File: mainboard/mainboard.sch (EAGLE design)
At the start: 12 parts, among them IC1 ATMEGA168-PU

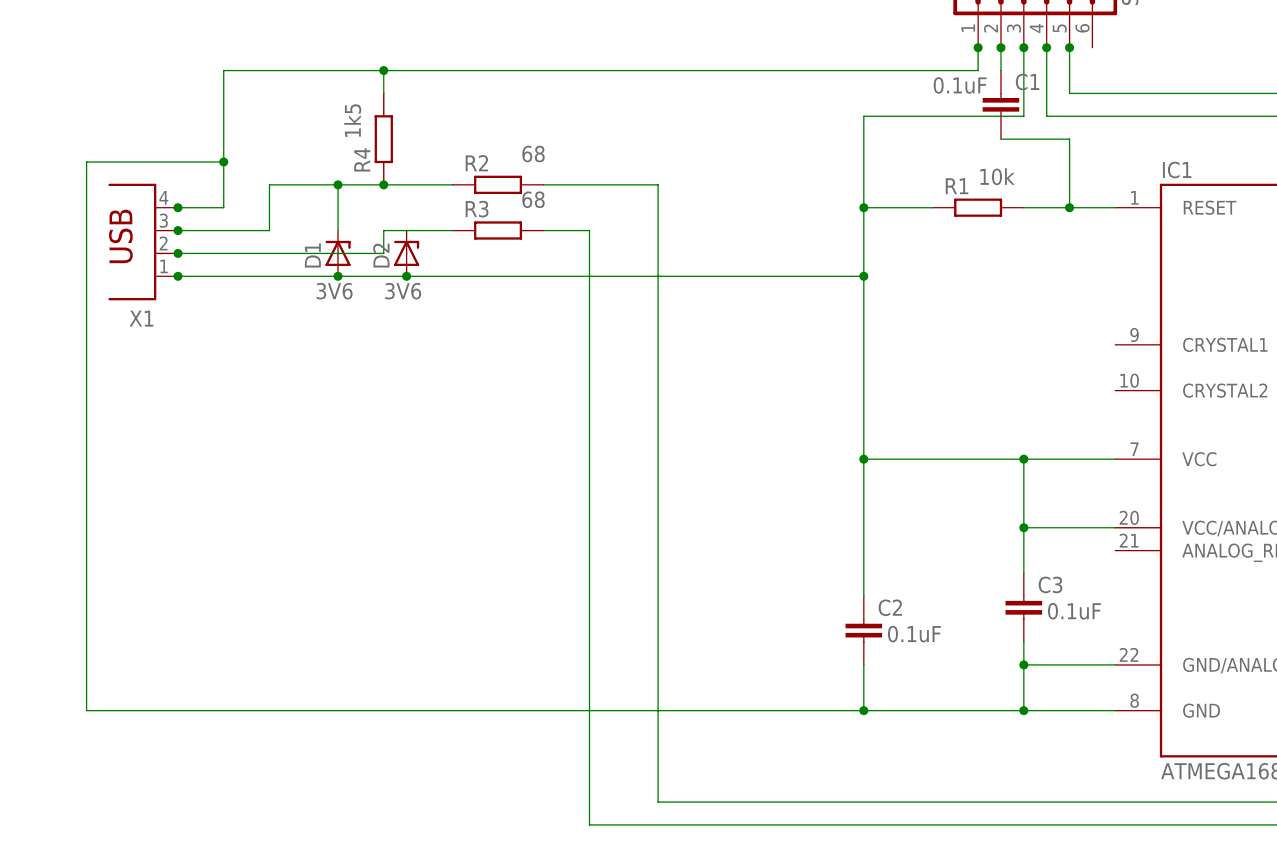
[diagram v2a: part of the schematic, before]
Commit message: added crystal, should run at 12mhz
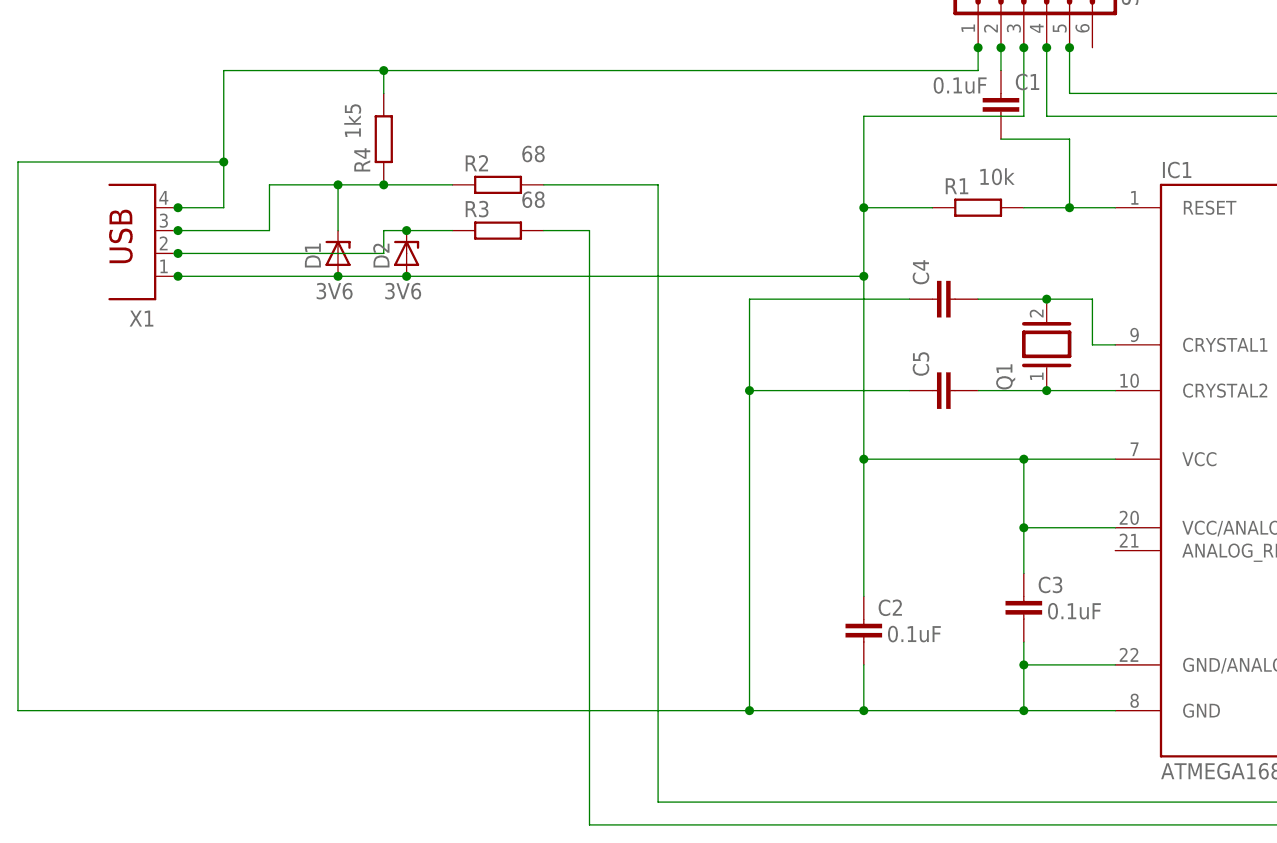
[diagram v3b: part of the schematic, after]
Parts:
- added C4, C5: (no value), capacitor-wima:C2,5-3
- added Q1: (no value), special:XTAL/S
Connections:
- new net N$12: C5.2, IC1.CRYSTAL2, Q1.1
- new net N$9: C2.2, C3.2, C4.1, C5.1, IC1.GND, IC1.GND/ANALOG, R4.2, SV1.1, X1.4
- net N$5: now also D2.C
- net N$8: now also C4.2, IC1.CRYSTAL1, Q1.2; no longer C2.2, C3.2, IC1.GND, IC1.GND/ANALOG, R4.2, SV1.1, X1.4

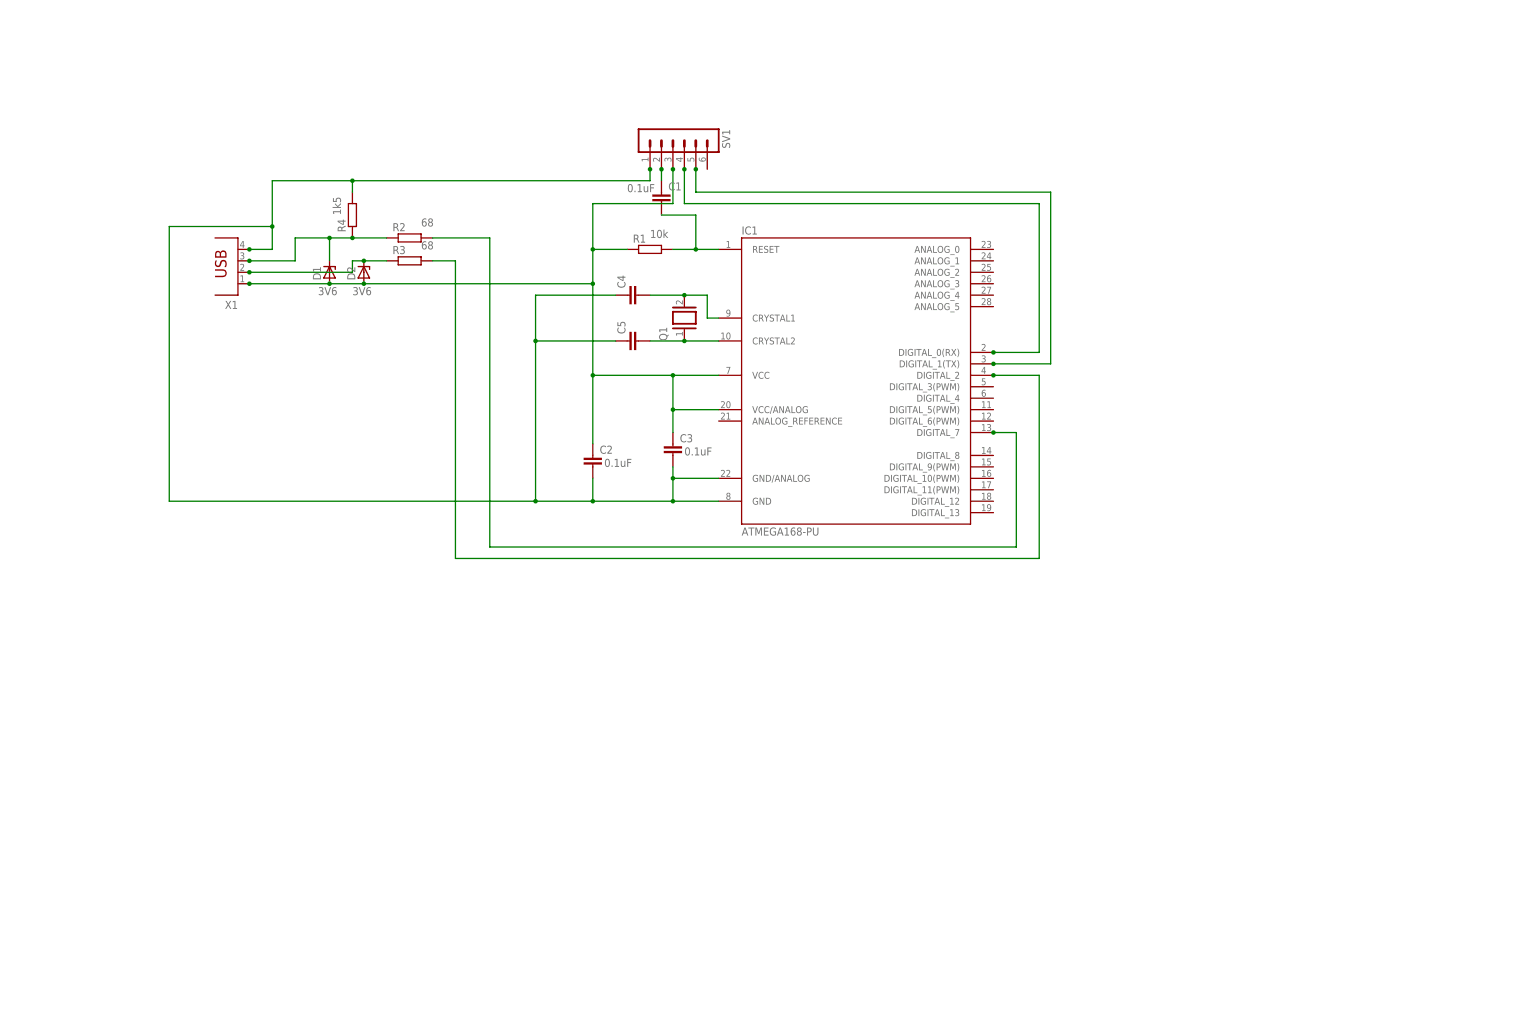
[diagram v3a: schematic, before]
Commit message: added optocouplers and screw terminals for ssr's
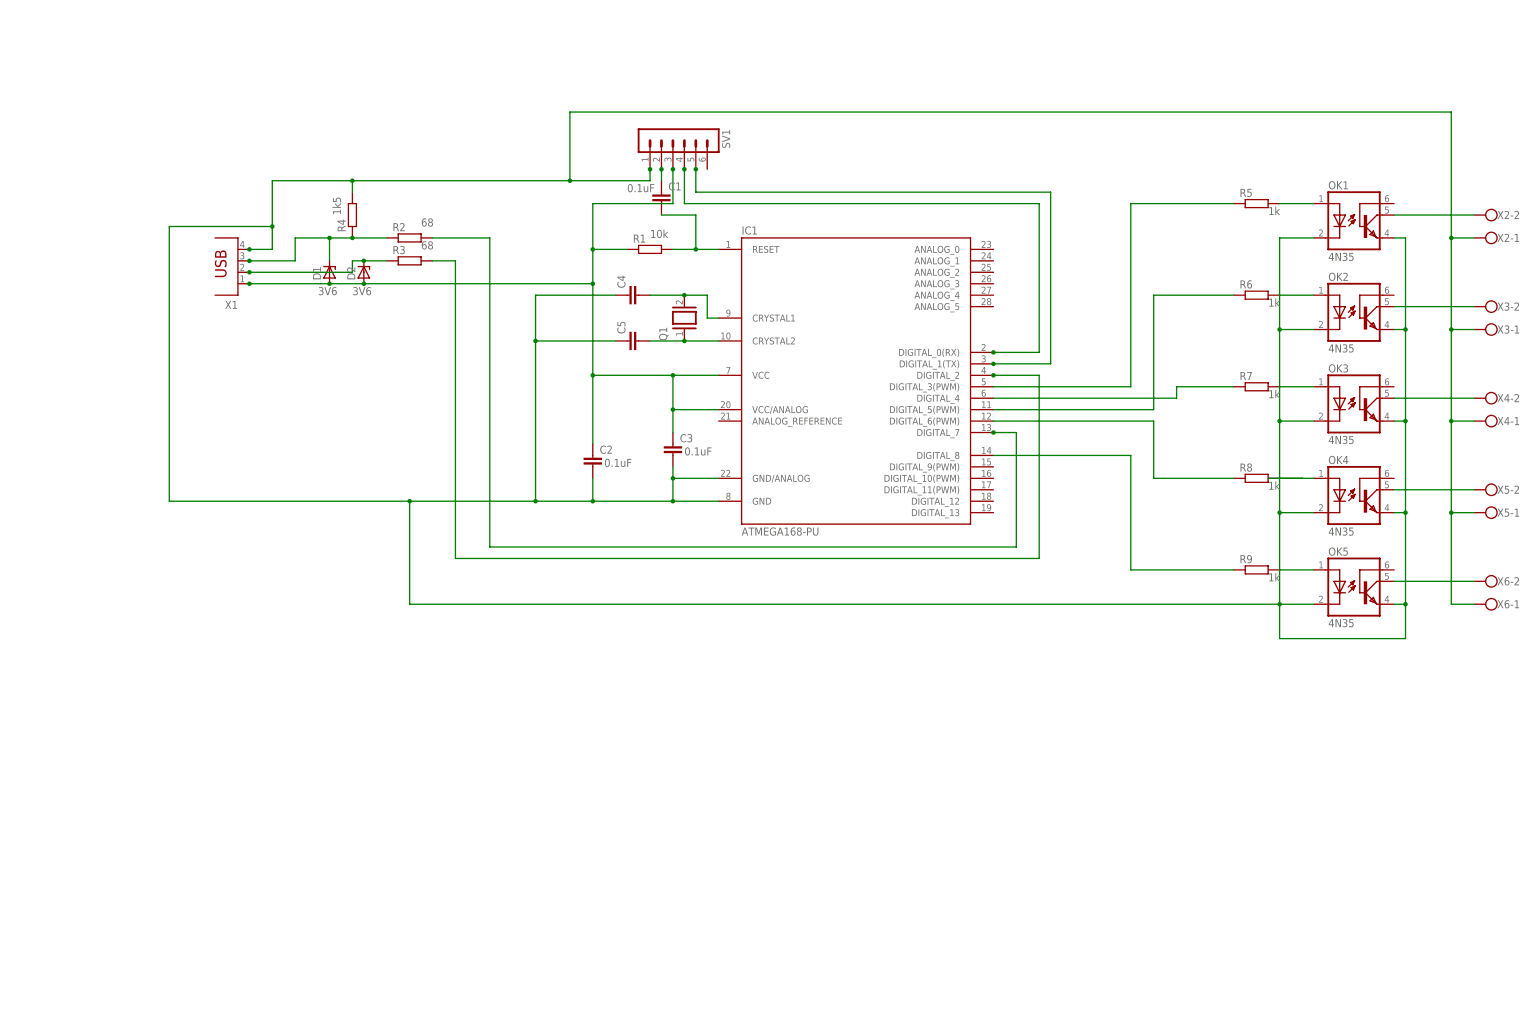
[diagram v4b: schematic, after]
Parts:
- added OK1, OK2, OK3, OK4, OK5: 4N35, optocoupler:4N35
- added R5, R6, R7, R8, R9: (no value), resistor:R-EU_0204/7
- added X2, X3, X4, X5, X6: (no value), con-wago-500:W237-102
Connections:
- new net N$13: IC1.DIGITAL_3(PWM), R5.1
- new net N$14: IC1.DIGITAL_5(PWM), R6.1
- new net N$15: IC1.DIGITAL_4, R7.1
- new net N$16: IC1.DIGITAL_6(PWM), R8.1
- new net N$17: IC1.DIGITAL_8, R9.1
- new net N$18: OK1.A, R5.2
- new net N$19: OK2.A, R6.2
- new net N$20: OK3.A, R7.2
- new net N$21: OK4.A, R8.2
- new net N$22: OK5.A, R9.2
- new net N$23: OK5.COL, X6-2.KL
- new net N$24: OK4.COL, X5-2.KL
- new net N$25: OK3.COL, X4-2.KL
- new net N$26: OK2.COL, X3-2.KL
- new net N$27: OK1.COL, X2-2.KL
- net N$9: now also OK1.C, OK1.EMI, OK2.C, OK2.EMI, OK3.C, OK3.EMI, OK4.C, OK4.EMI, OK5.C, OK5.EMI, X2-1.KL, X3-1.KL, X4-1.KL, X5-1.KL, X6-1.KL
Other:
- note added: "1k"

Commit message: added thermocouple interface chips and terminals
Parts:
- added C6: (no value), resistor:CPOL-EU153CLV-0605
- added C7: (no value), capacitor-wima:C2,5-3
- added D3, D4, D5, D6, D7: 1N4148DO35-7, diode:1N4148DO35-7
- added IC2, IC3, IC4, IC5: (no value), ic-package:DIL8S
- added IC6: LM317MSTT3, v-reg-mod:LM317MSTT3
- added R10, R11, R12, R13, R14: (no value), resistor:R-EU_0204/7
- added X10, X7, X8, X9: (no value), con-wago-500:W237-102
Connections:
- new net N$28: IC2.2, X7-1.KL
- new net N$29: C2.2, C3.2, C4.1, C5.1, C6.-, C7.2, IC1.GND, IC1.GND/ANALOG, IC2.1, IC3.1, IC4.1, IC5.1, IC6.ADJ, OK1.C, OK1.EMI, OK2.C, OK2.EMI, OK3.C, OK3.EMI, OK4.C, OK4.EMI, OK5.C, OK5.EMI, R4.2, SV1.1, X1.4
- new net N$30: C6.+, IC2.4, IC3.4, IC4.4, IC5.4, IC6.OUT, R10.2, R11.2, R12.2, R13.2, R14.2
- new net N$31: IC3.3, X8-2.KL
- new net N$32: IC4.3, X9-2.KL
- new net N$33: IC5.3, X10-2.KL
- new net N$34: IC3.2, X8-1.KL
- new net N$35: IC4.2, X9-1.KL
- new net N$36: IC5.2, X10-1.KL
- new net N$37: D3.A, IC2.5, IC3.5, IC4.5, IC5.5, R10.1
- new net N$38: D3.C, IC1.DIGITAL_9(PWM)
- new net N$39: D5.A, IC3.6, R12.1
- new net N$40: D4.A, IC2.6, R11.1
- new net N$41: D6.A, IC4.6, R13.1
- new net N$42: D7.A, IC5.6, R14.1
- new net N$43: D4.C, IC1.DIGITAL_13
- new net N$44: D5.C, IC1.DIGITAL_12
- new net N$45: D6.C, IC1.DIGITAL_11(PWM)
- new net N$46: D7.C, IC1.DIGITAL_10(PWM)
- new net N$47: IC1.ANALOG_0, IC2.7
- new net N$48: IC1.ANALOG_1, IC3.7
- new net N$49: IC1.ANALOG_2, IC4.7
- new net N$50: IC1.ANALOG_3, IC5.7
- net N$3: now also C7.1, IC6.IN, X2-1.KL, X3-1.KL, X4-1.KL, X5-1.KL, X6-1.KL
- net N$9: now also IC2.3, X7-2.KL; no longer C2.2, C3.2, C4.1, C5.1, IC1.GND, IC1.GND/ANALOG, OK1.C, OK1.EMI, OK2.C, OK2.EMI, OK3.C, OK3.EMI, OK4.C, OK4.EMI, OK5.C, OK5.EMI, R4.2, SV1.1, X1.4, X2-1.KL, X3-1.KL, X4-1.KL, X5-1.KL, X6-1.KL
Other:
- note added: "MAX31885 (SO->DIP)"
